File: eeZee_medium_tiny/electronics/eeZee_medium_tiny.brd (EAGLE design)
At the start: 28.7 x 16.3 mm, 11 parts, among them IC1 TINY24/44/84, J2 avrisp, Q1 16MHz

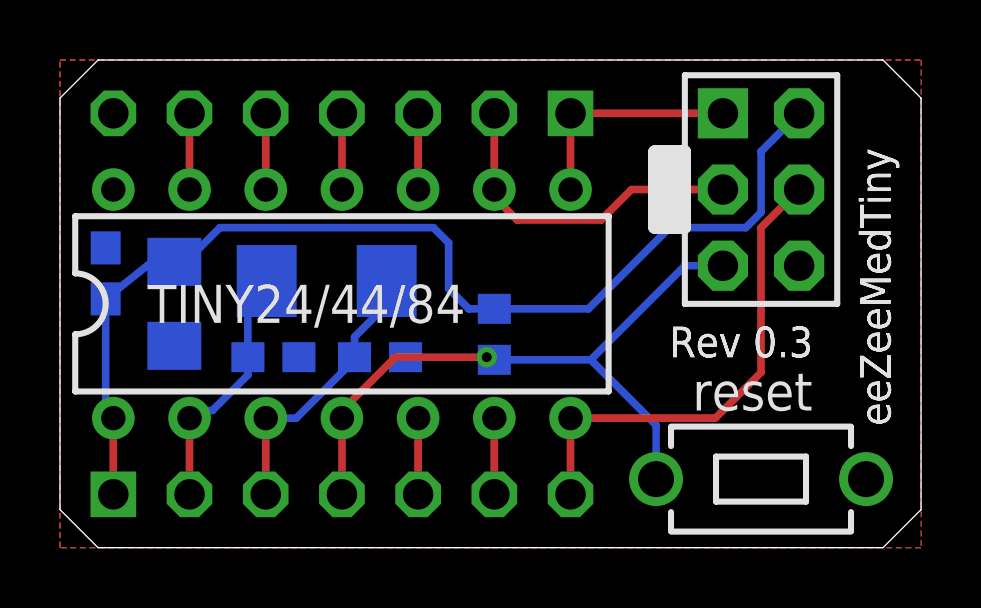
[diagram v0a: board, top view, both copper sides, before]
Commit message: Changed spacing to 10mil/8mil, relocated too-close traces, relocated via
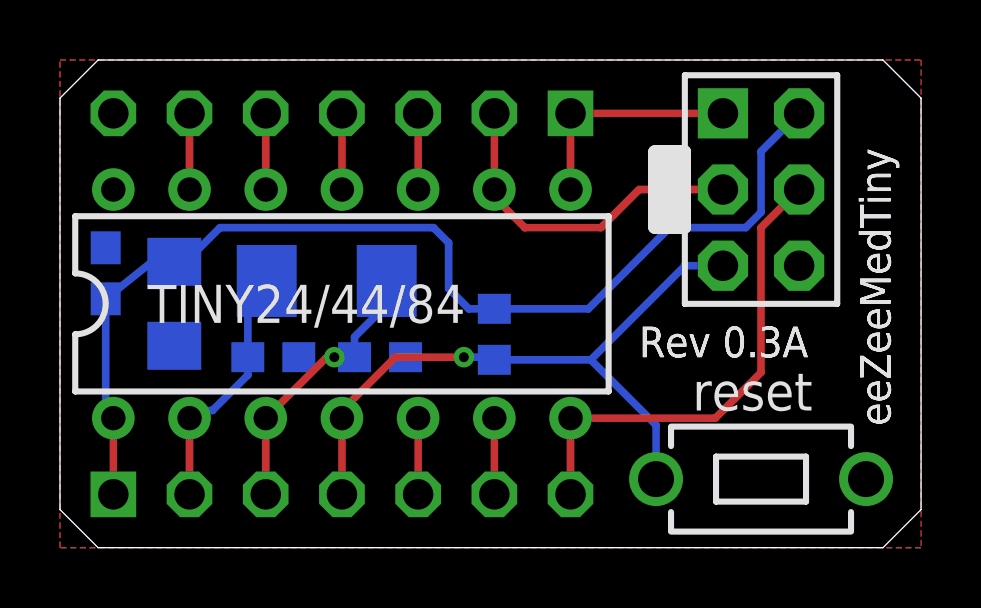
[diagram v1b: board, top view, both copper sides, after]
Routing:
- net XTAL2: track 9.38 -> 9.33 mm, vias 0 -> 1
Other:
- board text added: "Rev 0.3A"
- board text removed: "Rev 0.3"
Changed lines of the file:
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@@
 <vertex x="17.5521875" y="7.832015625"/>
 </polygon>
-<text x="20.32" y="6.35" size="1.016" layer="25" font="vector">Rev 0.3</text>
+<text x="19.304" y="6.35" size="1.016" layer="25" font="vector">Rev 0.3A</text>
 <text x="27.686" y="4.064" size="1.016" layer="25" font="vector" rot="R90">eeZeeMedTiny</text>
 <wire x1="24.814809375" y1="2.363190625" x2="21.921190625" y2="2.363190625" width="0.2032" layer="22"/>
@@
 <vertex x="17.5521875" y="7.8320125"/>
 </polygon>
-<text x="20.32" y="6.35" size="1.016" layer="121" font="vector" ratio="20">Rev 0.3</text>
+<text x="19.304" y="6.35" size="1.016" layer="121" font="vector" ratio="20">Rev 0.3A</text>
 <text x="27.686" y="4.064" size="1.016" layer="121" font="vector" ratio="20" rot="R90">eeZeeMedTiny</text>
 <text x="26.924" y="4.064" size="0.8128" layer="122" font="vector" ratio="25" rot="MR90">bot-thoughts.com</text>
@@
 </class>
 </classes>
-<designrules name="default *">
+<designrules name="LaenPCBOrder *">
 <description language="de">&lt;b&gt;EAGLE Design Rules&lt;/b&gt;
 &lt;p&gt;
@@
 <param name="mtCopper" value="0.0356mm 0.0356mm 0.0356mm 0.0356mm 0.0356mm 0.0356mm 0.0356mm 0.0356mm 0.0356mm 0.0356mm 0.0356mm 0.0356mm 0.0356mm 0.0356mm 0.0356mm 0.0356mm"/>
 <param name="mtIsolate" value="1.5011mm 0.1499mm 0.2007mm 0.1499mm 0.2007mm 0.1499mm 0.2007mm 0.1499mm 0.2007mm 0.1499mm 0.2007mm 0.1499mm 0.2007mm 0.1499mm 0.2007mm"/>
-<param name="mdWireWire" value="6mil"/>
-<param name="mdWirePad" value="6mil"/>
-<param name="mdWireVia" value="6mil"/>
-<param name="mdPadPad" value="6mil"/>
-<param name="mdPadVia" value="6mil"/>
-<param name="mdViaVia" value="6mil"/>
-<param name="mdSmdPad" value="6mil"/>
+<param name="mdWireWire" value="10mil"/>
+<param name="mdWirePad" value="10mil"/>
+<param name="mdWireVia" value="10mil"/>
+<param name="mdPadPad" value="10mil"/>
+<param name="mdPadVia" value="10mil"/>
+<param name="mdViaVia" value="10mil"/>
+<param name="mdSmdPad" value="0mil"/>
 <param name="mdSmdVia" value="0mil"/>
-<param name="mdSmdSmd" value="6mil"/>
+<param name="mdSmdSmd" value="8mil"/>
 <param name="mdViaViaSameLayer" value="8mil"/>
 <param name="mnLayersViaInSmd" value="2"/>
 <param name="mdCopperDimension" value="10mil"/>
-<param name="mdDrill" value="6mil"/>
+<param name="mdDrill" value="10mil"/>
 <param name="mdSmdStop" value="0mil"/>
 <param name="msWidth" value="6mil"/>
@@
 <param name="psTop" value="1"/>
 <param name="psBottom" value="1"/>
-<param name="psFirst" value="-1"/>
-<param name="psElongationLong" value="60"/>
-<param name="psElongationOffset" value="60"/>
+<param name="psFirst" value="1"/>
+<param name="psElongationLong" value="100"/>
+<param name="psElongationOffset" value="100"/>
 <param name="mvStopFrame" value="1"/>
 <param name="mvCreamFrame" value="0"/>
-<param name="mlMinStopFrame" value="4mil"/>
-<param name="mlMaxStopFrame" value="4mil"/>
+<param name="mlMinStopFrame" value="3mil"/>
+<param name="mlMaxStopFrame" value="3mil"/>
 <param name="mlMinCreamFrame" value="0mil"/>
 <param name="mlMaxCreamFrame" value="0mil"/>
-<param name="mlViaStopLimit" value="21mil"/>
+<param name="mlViaStopLimit" value="20mil"/>
 <param name="srRoundness" value="0"/>
 <param name="srMinRoundness" value="0mil"/>
@@
 <wire x1="9.398" y1="4.318" x2="9.398" y2="4.572" width="0.254" layer="1"/>
 <wire x1="9.398" y1="4.572" x2="11.176" y2="6.35" width="0.254" layer="1"/>
-<wire x1="11.176" y1="6.35" x2="14.224" y2="6.35" width="0.254" layer="1"/>
-<via x="14.224" y="6.35" extent="1-16" drill="0.3302"/>
-<wire x1="14.224" y1="6.35" x2="14.39" y2="6.35" width="0.254" layer="16"/>
+<wire x1="11.176" y1="6.35" x2="13.462" y2="6.35" width="0.254" layer="1"/>
+<via x="13.462" y="6.35" extent="1-16" drill="0.3302"/>
+<wire x1="13.462" y1="6.35" x2="14.39" y2="6.35" width="0.254" layer="16"/>
 <wire x1="14.39" y1="6.35" x2="14.478" y2="6.262" width="0.254" layer="16"/>
 <wire x1="14.478" y1="6.262" x2="17.692" y2="6.262" width="0.254" layer="16"/>
@@
 <wire x1="10.668" y1="7.874" x2="10.668" y2="8.668" width="0.254" layer="16"/>
 <wire x1="10.668" y1="8.668" x2="10.89" y2="8.89" width="0.254" layer="16"/>
-<wire x1="9.818" y1="6.35" x2="9.818" y2="6.262" width="0.254" layer="16"/>
-<wire x1="9.818" y1="6.262" x2="7.874" y2="4.318" width="0.254" layer="16"/>
-<wire x1="7.874" y1="4.318" x2="6.858" y2="4.318" width="0.254" layer="16"/>
+<wire x1="6.858" y1="4.318" x2="8.89" y2="6.35" width="0.254" layer="1"/>
+<wire x1="8.89" y1="6.35" x2="9.144" y2="6.35" width="0.254" layer="1"/>
+<via x="9.144" y="6.35" extent="1-16" drill="0.3302"/>
+<wire x1="9.144" y1="6.35" x2="9.818" y2="6.35" width="0.254" layer="16"/>
 </signal>
 <signal name="XTAL1">
@@
 <wire x1="14.478" y1="14.478" x2="14.478" y2="11.938" width="0.254" layer="1"/>
 <wire x1="14.478" y1="11.938" x2="14.478" y2="11.684" width="0.254" layer="1"/>
-<wire x1="14.478" y1="11.684" x2="15.24" y2="10.922" width="0.254" layer="1"/>
-<wire x1="15.24" y1="10.922" x2="18.034" y2="10.922" width="0.254" layer="1"/>
-<wire x1="18.034" y1="10.922" x2="19.05" y2="11.938" width="0.254" layer="1"/>
-<wire x1="19.05" y1="11.938" x2="22.098" y2="11.938" width="0.254" layer="1"/>
+<wire x1="14.478" y1="11.684" x2="15.494" y2="10.668" width="0.254" layer="1"/>
+<wire x1="15.494" y1="10.668" x2="18.034" y2="10.668" width="0.254" layer="1"/>
+<wire x1="18.034" y1="10.668" x2="19.304" y2="11.938" width="0.254" layer="1"/>
+<wire x1="19.304" y1="11.938" x2="22.098" y2="11.938" width="0.254" layer="1"/>
 </signal>
 <signal name="N$8">
